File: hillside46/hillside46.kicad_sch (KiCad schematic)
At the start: 92 parts, among them J1 Haptic, J2 TRRS, J3 Bat_Pos, J4 Bat_Neg, J5 Bat_Pos, J6 Bat_Neg, K1 SW_Key, K10 SW_Key, K11 SW_Key, K12 SW_Key, K13 SW_Key, K14 SW_Key, K15 SW_Key, K16 SW_Key, K17 SW_Key, K18 SW_Key, K19 SW_Rotary, K2 SW_Key, K20 SW_Rotary, K21 SW_Key, K22 SW_Key, K23 SW_Key, K3 SW_Key, K4 SW_Key, K5 SW_Key, K6 SW_Key, K7 SW_Key, K8 SW_Key, K9 SW_Key, SW1 SKQGAFE010, SW2 SW_Power, U1 ProMicro_r, U2 SRV05-4

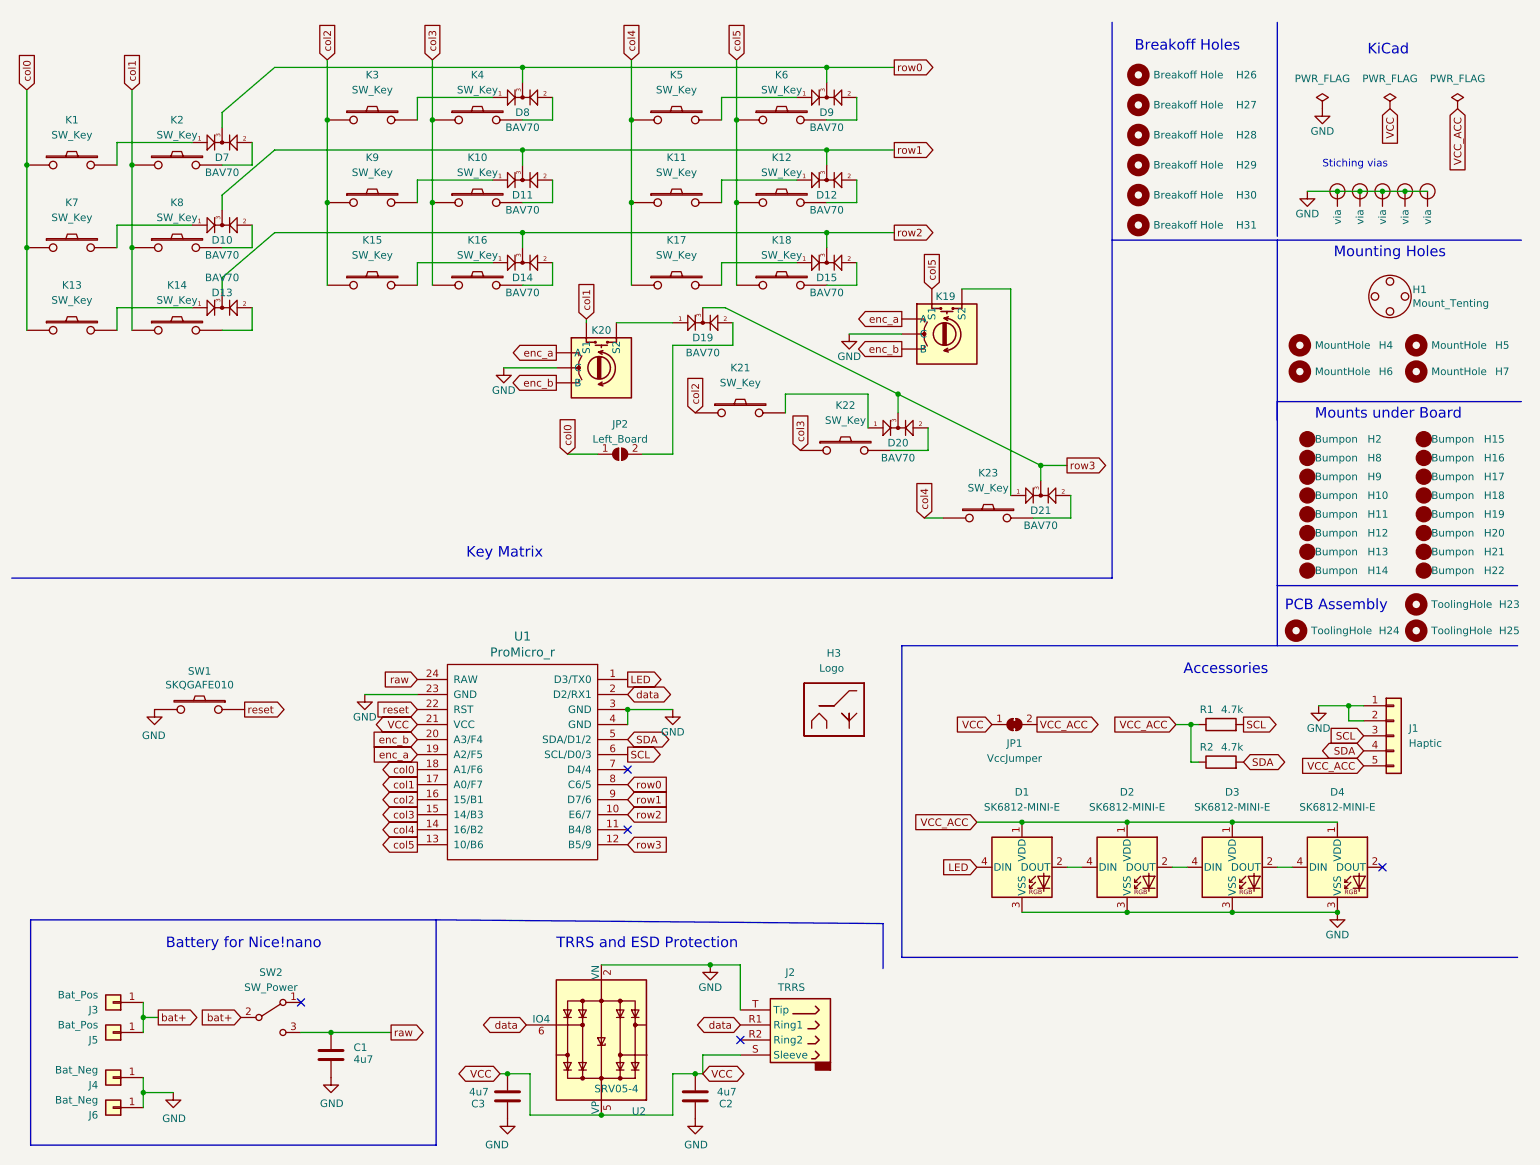
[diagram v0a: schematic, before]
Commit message: Adding nice view footprints and removing old haptic buzzer, I2C pullup resistors and all LEDs
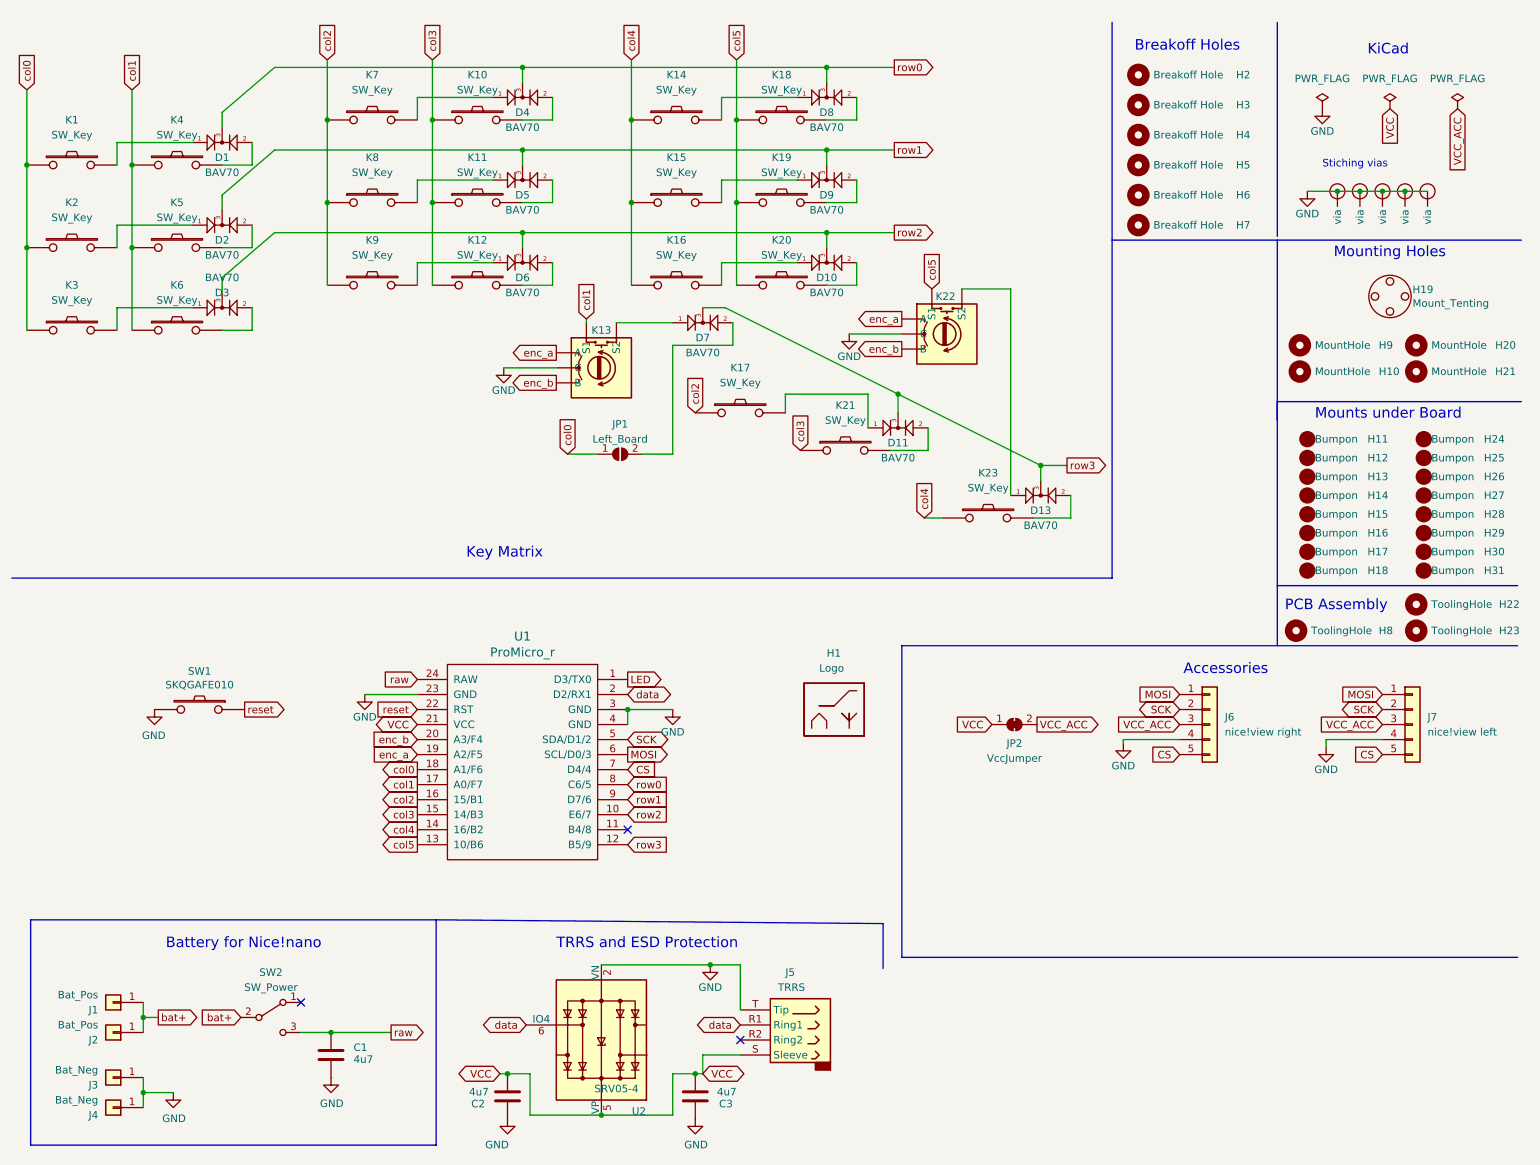
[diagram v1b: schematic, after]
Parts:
- removed D1, D2, D3, D4: SK6812-MINI-E, hillside_basic:SK6812-MINI-E, symbol hillside_basic:SK6812-MINI-E
- removed R1, R2: 4.7k, hillside_basic:R_0805_2012Metric, symbol Device:R
- added J7: nice!view left, hillside:nice_view, symbol Connector_Generic:Conn_01x05
- J6: renamed from J1; value Haptic -> nice!view right; footprint hillside:Pimoroni_Haptic -> hillside:nice_view
- renumbered C3 to C2, C2 to C3, D7 to D1, D15 to D10, D20 to D11, D21 to D13, D10 to D2, D13 to D3, D8 to D4, D11 to D5, D14 to D6, D19 to D7, D9 to D8, D12 to D9, H3 to H1, H6 to H10, H2 to H11, H8 to H12, H9 to H13, H10 to H14, H11 to H15, H12 to H16, H13 to H17, H14 to H18, H1 to H19, H26 to H2, H5 to H20, H7 to H21, H23 to H22, H25 to H23, H15 to H24, H16 to H25, H17 to H26, H18 to H27, H19 to H28, H20 to H29, H27 to H3, H21 to H30, H22 to H31, H28 to H4, H29 to H5, H30 to H6, H31 to H7, H24 to H8, H4 to H9, J3 to J1, J5 to J2, J4 to J3, J6 to J4, J2 to J5, JP2 to JP1, JP1 to JP2, K4 to K10, K10 to K11, K16 to K12, K20 to K13, K5 to K14, K11 to K15, K17 to K16, K21 to K17, K6 to K18, K12 to K19, K7 to K2, K18 to K20, K22 to K21, K19 to K22, K13 to K3, K2 to K4, K8 to K5, K14 to K6, K3 to K7, K9 to K8, K15 to K9
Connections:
- net GND: now also J6.4 (Pin_4), J7.4 (Pin_4); no longer J6.1 (Pin_1), J6.2 (Pin_2)
- net VCC_ACC: now also J6.3 (Pin_3), J7.3 (Pin_3); no longer J6.5 (Pin_5)
- net CS: now reaches U1.7 (D4/4)
- net CS: now also J6.5 (Pin_5), J7.5 (Pin_5)
- net SCL renamed MOSI
- net MOSI: now also J6.1 (Pin_1), J7.1 (Pin_1); no longer J6.3 (Pin_3)
- net SDA renamed SCK
- net SCK: now also J6.2 (Pin_2), J7.2 (Pin_2); no longer J6.4 (Pin_4)
- no-connect marks 5 -> 3
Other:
- moved on the sheet: J6
